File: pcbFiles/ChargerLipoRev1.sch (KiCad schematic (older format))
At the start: 6 parts

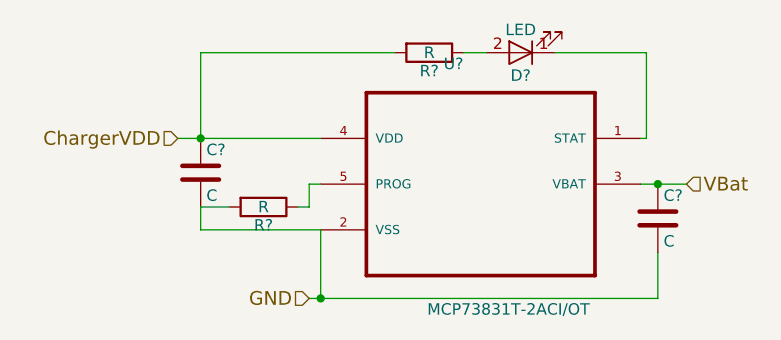
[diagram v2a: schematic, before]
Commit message: Update Footprints and Board Layers
Still need to get foorprint for x... device and the lpf may need to make them if I cannot find them @willcarroll7
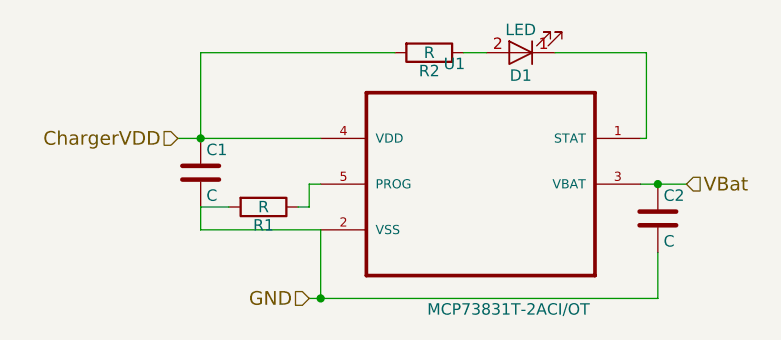
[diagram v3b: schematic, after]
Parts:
- C1, C2: renamed from C?; footprint (none) -> Capacitors_SMD:C_0402
- D1: renamed from D?; footprint (none) -> Capacitors_SMD:C_0603
- R1, R2: renamed from R?; footprint (none) -> Resistors_SMD:R_0402
- U1: renamed from U?; footprint SOT95P280X145-5N -> MCP73831T-2ACI_OT:SOT95P280X145-5N
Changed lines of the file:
@@
-EESchema Schematic File Version 4
+EESchema Schematic File Version 2
 LIBS:power
+LIBS:device
+LIBS:switches
+LIBS:relays
+LIBS:motors
+LIBS:transistors
+LIBS:conn
+LIBS:linear
+LIBS:regul
 LIBS:74xx
+LIBS:cmos4000
+LIBS:adc-dac
+LIBS:memory
+LIBS:xilinx
+LIBS:microcontrollers
+LIBS:dsp
+LIBS:microchip
+LIBS:analog_switches
+LIBS:motorola
+LIBS:texas
+LIBS:intel
+LIBS:audio
+LIBS:interface
+LIBS:digital-audio
+LIBS:philips
+LIBS:display
+LIBS:cypress
+LIBS:siliconi
+LIBS:opto
+LIBS:atmel
+LIBS:contrib
+LIBS:valves
+LIBS:ADS1115IDGST
+LIBS:CYW20719B1KUMLG
+LIBS:LSM9DS1TR
+LIBS:TPS63001DRCT
+LIBS:MCP73831T-2ACI_OT
+LIBS:A-1JB
+LIBS:XC6119N16A7R-G
 LIBS:GolfGloveMainBoardV1.0.0-cache
-EELAYER 26 0
+EELAYER 25 0
 EELAYER END
 $Descr A4 11693 8268
@@
 $EndDescr
 $Comp
-L MCP73831T-2ACI/OT U?
+L MCP73831T-2ACI/OT U1
 U 1 1 5C49B798
 P 5225 3250
-F 0 "U?" H 5063 3647 50  0000 L BNN
+F 0 "U1" H 5063 3647 50  0000 L BNN
 F 1 "MCP73831T-2ACI/OT" H 4991 2573 50  0000 L BNN
-F 2 "SOT95P280X145-5N" H 5225 3250 50  0001 L BNN
+F 2 "MCP73831T-2ACI_OT:SOT95P280X145-5N" H 5225 3250 50  0001 L BNN
 F 3 "SOT-23 Microchip" H 5225 3250 50  0001 L BNN
 F 4 "MCP73831T-2ACI/OT" H 5225 3250 50  0001 L BNN "Field4"
@@
 $EndComp
 $Comp
-L R R?
+L R R1
 U 1 1 5C49B813
 P 4275 3450
-F 0 "R?" V 4355 3450 50  0000 C CNN
+F 0 "R1" V 4355 3450 50  0000 C CNN
 F 1 "R" V 4275 3450 50  0000 C CNN
-F 2 "" V 4205 3450 50  0001 C CNN
+F 2 "Resistors_SMD:R_0402" V 4205 3450 50  0001 C CNN
 F 3 "" H 4275 3450 50  0001 C CNN
 	1    4275 3450
@@
 $EndComp
 $Comp
-L R R?
+L R R2
 U 1 1 5C49B864
 P 5000 2775
-F 0 "R?" V 5080 2775 50  0000 C CNN
+F 0 "R2" V 5080 2775 50  0000 C CNN
 F 1 "R" V 5000 2775 50  0000 C CNN
-F 2 "" V 4930 2775 50  0001 C CNN
+F 2 "Resistors_SMD:R_0402" V 4930 2775 50  0001 C CNN
 F 3 "" H 5000 2775 50  0001 C CNN
 	1    5000 2775
@@
 $EndComp
 $Comp
-L C C?
+L C C1
 U 1 1 5C49B8A9
 P 4000 3300
-F 0 "C?" H 4025 3400 50  0000 L CNN
+F 0 "C1" H 4025 3400 50  0000 L CNN
 F 1 "C" H 4025 3200 50  0000 L CNN
-F 2 "" H 4038 3150 50  0001 C CNN
+F 2 "Capacitors_SMD:C_0402" H 4038 3150 50  0001 C CNN
 F 3 "" H 4000 3300 50  0001 C CNN
 	1    4000 3300
@@
 $EndComp
 $Comp
-L C C?
+L C C2
 U 1 1 5C49B8F8
 P 6000 3500
-F 0 "C?" H 6025 3600 50  0000 L CNN
+F 0 "C2" H 6025 3600 50  0000 L CNN
 F 1 "C" H 6025 3400 50  0000 L CNN
-F 2 "" H 6038 3350 50  0001 C CNN
+F 2 "Capacitors_SMD:C_0402" H 6038 3350 50  0001 C CNN
 F 3 "" H 6000 3500 50  0001 C CNN
 	1    6000 3500
@@
 $EndComp
 $Comp
-L LED D?
+L LED D1
 U 1 1 5C49B969
 P 5400 2775
-F 0 "D?" H 5400 2875 50  0000 C CNN
+F 0 "D1" H 5400 2875 50  0000 C CNN
 F 1 "LED" H 5400 2675 50  0000 C CNN
-F 2 "" H 5400 2775 50  0001 C CNN
+F 2 "Capacitors_SMD:C_0603" H 5400 2775 50  0001 C CNN
 F 3 "" H 5400 2775 50  0001 C CNN
 	1    5400 2775

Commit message: Update the Voltage Detector Footprint
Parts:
- U1: footprint MCP73831T-2ACI_OT:SOT95P280X145-5N -> Buttons_Switches_SMD:SW_DIP_x1_W8.61mm_Slide_LowProfile
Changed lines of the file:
@@
 F 0 "U1" H 5063 3647 50  0000 L BNN
 F 1 "MCP73831T-2ACI/OT" H 4991 2573 50  0000 L BNN
-F 2 "MCP73831T-2ACI_OT:SOT95P280X145-5N" H 5225 3250 50  0001 L BNN
+F 2 "Buttons_Switches_SMD:SW_DIP_x1_W8.61mm_Slide_LowProfile" H 5225 3250 50  0001 L BNN
 F 3 "SOT-23 Microchip" H 5225 3250 50  0001 L BNN
 F 4 "MCP73831T-2ACI/OT" H 5225 3250 50  0001 L BNN "Field4"

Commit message: Update Circuit With Antenna
This commit will update the pcb with a mock up of the antenna design without the vias, this commit will also update the pressure sensors to be attached to the top of hand unit to allow for USB-C Connection. @willcarroll7
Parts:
- U1: footprint Buttons_Switches_SMD:SW_DIP_x1_W8.61mm_Slide_LowProfile -> MCP73831T-2ACI_OT:SOT95P280X145-5N
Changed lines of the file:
@@
 LIBS:valves
 LIBS:2450AT42B100E
+LIBS:A-1JB
+LIBS:ADS1115IDGST
+LIBS:CD4011BM96
+LIBS:CYW20719B1KUMLG
+LIBS:LSM9DS1TR
+LIBS:MCP73831T-2ACI_OT
+LIBS:MMDT3904V-7
+LIBS:MMPQ3904
+LIBS:S2B-PH-K-S_LF__SN_
+LIBS:TPS63001DRCT
+LIBS:XC6119N16A7R-G
 LIBS:GolfGloveMainBoardV1.0.0-cache
 EELAYER 25 0
@@
 F 0 "U1" H 5063 3647 50  0000 L BNN
 F 1 "MCP73831T-2ACI/OT" H 4991 2573 50  0000 L BNN
-F 2 "Buttons_Switches_SMD:SW_DIP_x1_W8.61mm_Slide_LowProfile" H 5225 3250 50  0001 L BNN
+F 2 "MCP73831T-2ACI_OT:SOT95P280X145-5N" H 5225 3250 50  0001 L BNN
 F 3 "SOT-23 Microchip" H 5225 3250 50  0001 L BNN
 F 4 "MCP73831T-2ACI/OT" H 5225 3250 50  0001 L BNN "Field4"
